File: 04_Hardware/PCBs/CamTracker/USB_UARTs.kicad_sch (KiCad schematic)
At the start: 36 parts, among them J3 67996-100HLF, J5 22-28-4034, J6 USB4080-03-A, Q7 BC817-40,215, U1 SC206EEMDA-G51-UGNDA, U7 PI3USB4000DZUAEX, U9 PI3USB4000DZUAEX

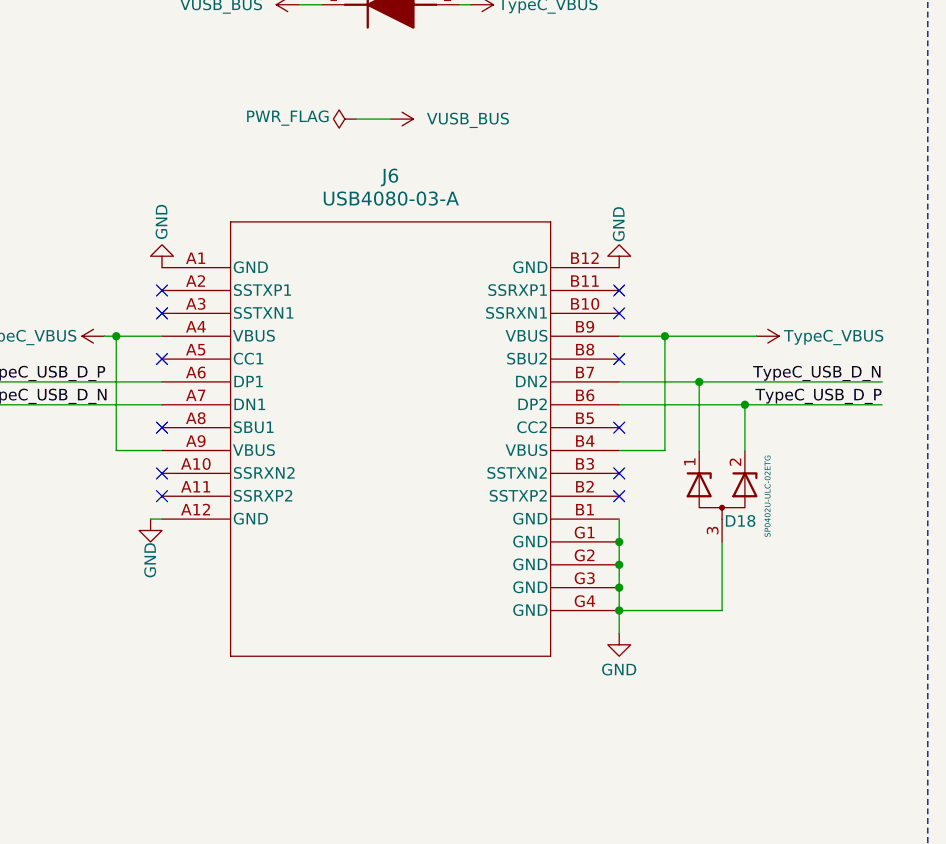
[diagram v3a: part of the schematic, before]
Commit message: feat(PCB): Added TE Connectivity connectors except the SD connector
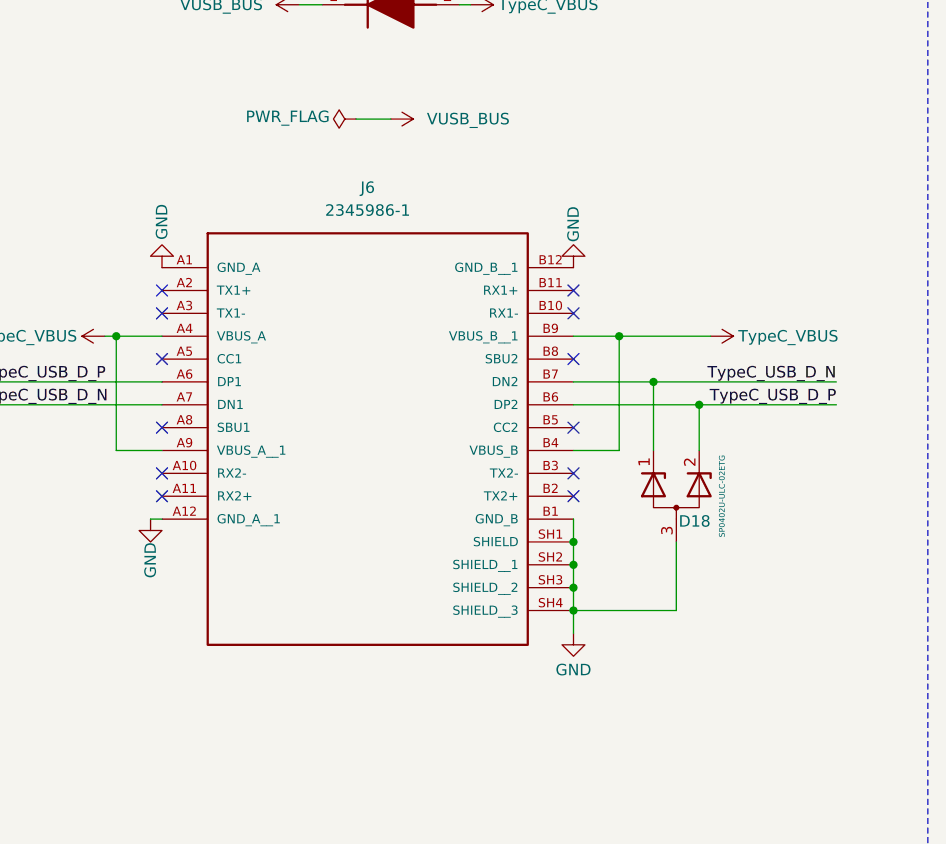
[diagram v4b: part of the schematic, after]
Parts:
- removed J6: USB4080-03-A, 000MCLib:GCT_USB4080-03-A_REVA, symbol 000MCLib:USB4080-03-A
- added J6: 2345986-1, 000MCLib:TE_2345986-1, symbol 000MCLib:2345986-1
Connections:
- net GND: now also J6.A1 (GND_A), J6.A12 (GND_A__1), J6.B1 (GND_B), J6.B12 (GND_B__1), J6.SH1 (SHIELD), J6.SH2 (SHIELD__1), J6.SH3 (SHIELD__2), J6.SH4 (SHIELD__3)
- net TypeC_USB_D_N: now also J6.A7 (DN1), J6.B7 (DN2)
- net TypeC_USB_D_P: now also J6.A6 (DP1), J6.B6 (DP2)
- net TypeC_VBUS: now also J6.A4 (VBUS_A), J6.A9 (VBUS_A__1), J6.B4 (VBUS_B), J6.B9 (VBUS_B__1)
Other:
- moved on the sheet: D18

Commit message: feat(PCB): finalize PCB design and generate BOM/Gerbers
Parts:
- added TP50: TestPoint, TestPoint:TestPoint_Pad_D1.0mm, symbol 000MCLib:TestPoint
- R20: Height 0.5 -> (none); Mouser Part Number 71-CRCW0805-0-E3 -> (none); Mouser Price/Stock https://www.mouser.co.uk/ProductDetail/Vishay-Dale/CRCW0805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 -> (none)
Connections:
- net NVMe_USB_Detect: now also TP50.1
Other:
- note added: "CC1=5K1 Pull-down ==> SC206 Host CC1=56K Pull-up ==> SC206 Device"

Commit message: feat(PCB): Updated NVME USB EN logic, turn-off the NVME 3V3 and 1V05 by EN pin
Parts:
- removed R18: 10K, 000MCLib:RC0402N_YAG, symbol 000MCLib:RC0402JR-0710KL
- added R112: 0R, 000MCLib:RESC2012X50N, symbol 000MCLib:CRCW08050000Z0EA
- added TP51: TestPoint, TestPoint:TestPoint_Pad_D1.0mm, symbol 000MCLib:TestPoint
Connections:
- net USB_SW: now also R112.1, TP51.1; no longer Q7.1 (B)
- net NVMe_USB_Detect renamed NVMe_USB_EN
- new net: Q7.1 (B), R112.2
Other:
- moved on the sheet: Q7, TP50
